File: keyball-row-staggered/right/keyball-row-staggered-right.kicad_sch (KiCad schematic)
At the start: 77 parts, among them J11 trackball, J12 MJ-4PP-9, SW1 SW_PUSH, SW10 SW_PUSH, SW11 SW_PUSH, SW12 SW_PUSH, SW13 SW_PUSH, SW14 SW_PUSH, SW15 SW_PUSH, SW16 SW_PUSH, SW17 SW_PUSH, SW18 SW_PUSH, SW19 SW_PUSH, SW2 SW_PUSH, SW20 SW_PUSH, SW21 SW_PUSH, SW22 SW_PUSH, SW23 SW_PUSH, SW24 SW_PUSH, SW25 SW_PUSH, SW26 SW_PUSH, SW27 SW_PUSH, SW28 SW_PUSH, SW29 SW_PUSH, SW3 SW_PUSH, SW30 SW_PUSH, SW31 SW_PUSH, SW32 SW_PUSH, SW33 SW_PUSH, SW34 SW_PUSH, SW4 SW_PUSH, SW5 SW_PUSH, SW6 SW_PUSH, SW7 SW_PUSH, SW8 SW_PUSH, SW9 SW_PUSH, U1 ProMicro

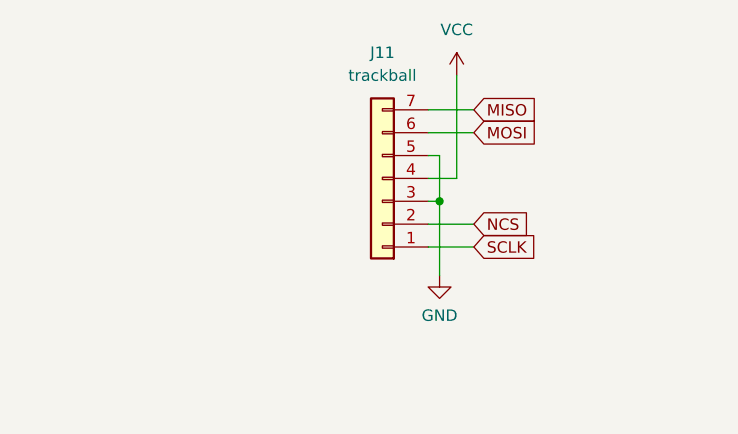
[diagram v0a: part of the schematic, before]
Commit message: キーボード側をtrackball基板に合わせて修正
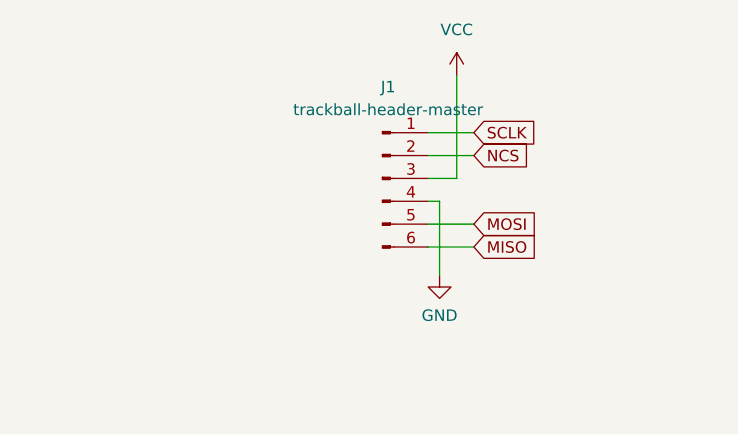
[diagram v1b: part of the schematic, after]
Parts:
- removed J11: trackball, tsuburin-keyboard:keyball_trackball, symbol Connector_Generic:Conn_01x07
- added J1: trackball-header-master, tsuburin-keyboard:keyball_trackball_header_master, symbol tsuburin-keyboard:trackball-header-master
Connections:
- net GND: now also J1.4 (GND)
- net MISO: now also J1.6 (MISO)
- net MOSI: now also J1.5 (MOSI)
- net NCS: now also J1.2 (NCS)
- net SCLK: now also J1.1 (SCLK)
- net VCC: now also J1.3 (VCC)
